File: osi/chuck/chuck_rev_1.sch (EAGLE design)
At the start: 3 parts

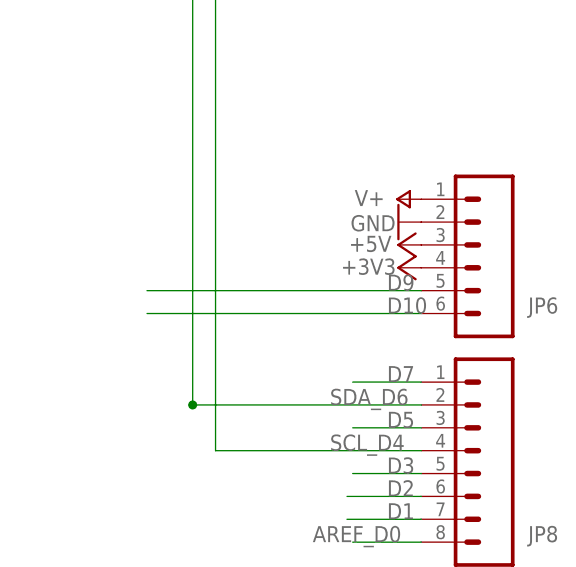
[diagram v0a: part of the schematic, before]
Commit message: D9 -> D8 for INT0
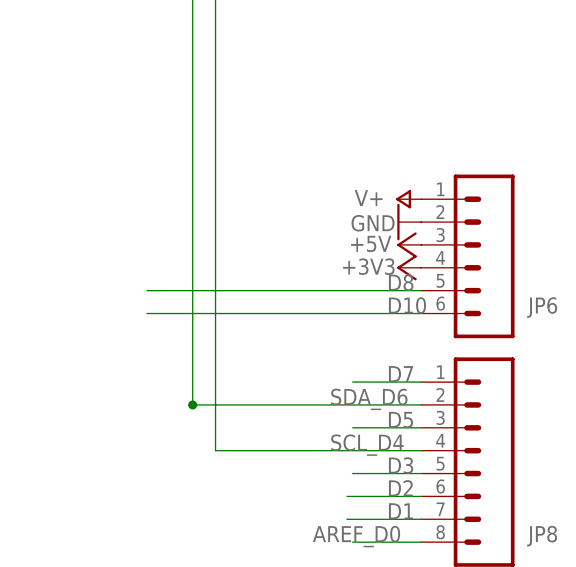
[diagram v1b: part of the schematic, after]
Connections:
- net D9 renamed D8
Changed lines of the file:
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@@
 </segment>
 </net>
-<net name="D9" class="0">
+<net name="D8" class="0">
 <segment>
 <wire x1="160.655" y1="86.36" x2="191.135" y2="86.36" width="0.1524" layer="91"/>

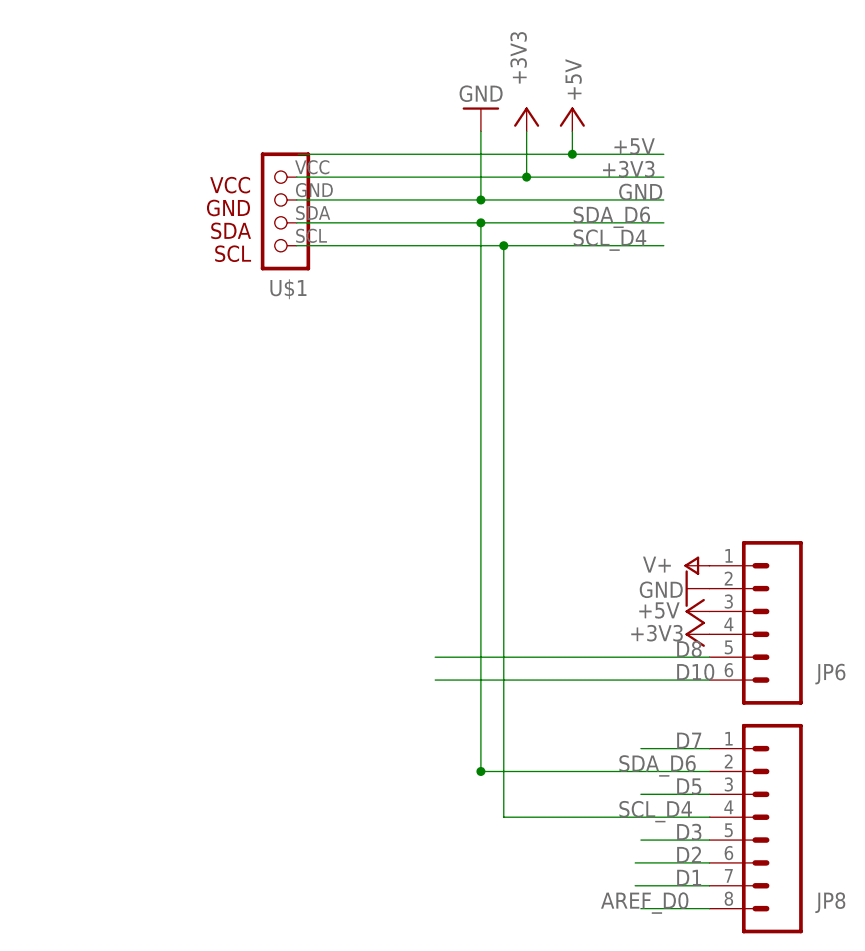
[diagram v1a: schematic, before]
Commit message: Moving RST line in brain
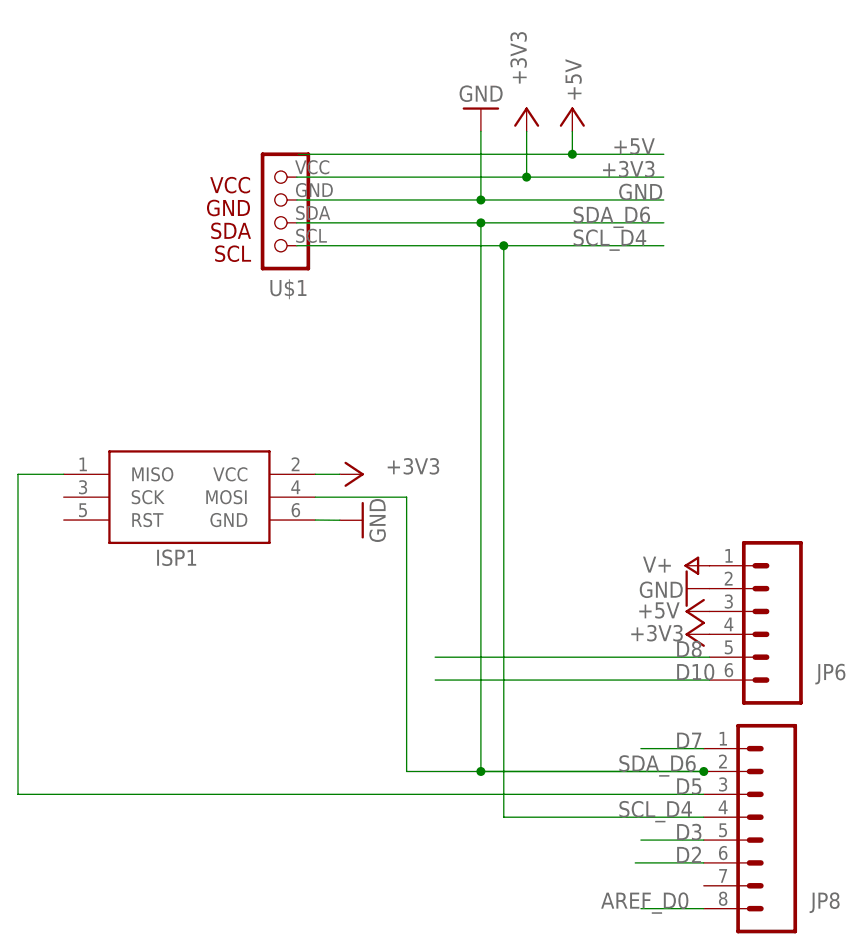
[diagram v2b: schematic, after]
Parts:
- added ISP1: AVRISP-6, adafruit_mod:AVRISP-6
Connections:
- removed net D1: JP8.7
- net +3V3: now also ISP1.VCC
- net D5: now also ISP1.MISO
- net GND: now also ISP1.GND
- net SDA_D6: now also ISP1.MOSI
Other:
- moved on the sheet: JP8
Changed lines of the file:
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@@
 <setting verticaltext="up"/>
 </settings>
-<grid distance="0.1" unitdist="inch" unit="inch" style="lines" multiple="1" display="no" altdistance="0.01" altunitdist="inch" altunit="inch"/>
+<grid distance="0.1" unitdist="inch" unit="inch" style="lines" multiple="1" display="no" altdistance="0.001" altunitdist="inch" altunit="inch"/>
 <layers>
 <layer number="1" name="Top" color="4" fill="1" visible="no" active="no"/>
@@
 <part name="FRAME1" library="SparkFun_mod" deviceset="FRAME-LETTER" device=""/>
 <part name="U$1" library="_my-parts" deviceset="NUNCHUCK" device="CHUCK"/>
+<part name="ISP1" library="adafruit_mod" deviceset="AVRISP" device="-6"/>
+<part name="+3V1" library="supply1" deviceset="+3V3" device=""/>
+<part name="GND1" library="SparkFun" deviceset="GND" device=""/>
 </parts>
 <sheets>
@@
 <attribute name="NAME" x="206.375" y="85.598" size="1.778" layer="95" rot="R180"/>
 </instance>
-<instance part="JP8" gate="G$1" x="196.215" y="68.58" smashed="yes" rot="R180">
-<attribute name="VALUE" x="201.295" y="81.28" size="1.778" layer="96" rot="R180"/>
-<attribute name="NAME" x="206.375" y="60.198" size="1.778" layer="95" rot="R180"/>
+<instance part="JP8" gate="G$1" x="195.58" y="68.58" smashed="yes" rot="R180">
+<attribute name="VALUE" x="200.66" y="81.28" size="1.778" layer="96" rot="R180"/>
+<attribute name="NAME" x="205.74" y="60.198" size="1.778" layer="95" rot="R180"/>
 </instance>
 <instance part="FRAME1" gate="G$1" x="0" y="0"/>
 <instance part="FRAME1" gate="G$2" x="147.32" y="0"/>
 <instance part="U$1" gate="G$1" x="147.828" y="142.24" rot="R180"/>
+<instance part="ISP1" gate="G$1" x="132.08" y="104.14"/>
+<instance part="+3V1" gate="G$1" x="152.6032" y="106.68" smashed="yes" rot="R270">
+<attribute name="VALUE" x="155.1432" y="106.68" size="1.778" layer="96"/>
+</instance>
+<instance part="GND1" gate="1" x="152.6032" y="101.5746" rot="R90"/>
 </instances>
 <busses>
@@
 <pinref part="JP6" gate="G$1" pin="2"/>
 </segment>
+<segment>
+<pinref part="ISP1" gate="G$1" pin="GND"/>
+<wire x1="147.32" y1="101.6" x2="150.0632" y2="101.5746" width="0.1524" layer="91"/>
+<pinref part="GND1" gate="1" pin="GND"/>
+</segment>
 </net>
 <net name="D3" class="0">
 <segment>
-<wire x1="191.135" y1="66.04" x2="183.515" y2="66.04" width="0.1524" layer="91"/>
+<wire x1="190.5" y1="66.04" x2="183.515" y2="66.04" width="0.1524" layer="91"/>
 <pinref part="JP8" gate="G$1" pin="5"/>
 <label x="187.325" y="66.04" size="1.778" layer="95"/>
@@
 <net name="D2" class="0">
 <segment>
-<wire x1="191.135" y1="63.5" x2="182.88" y2="63.5" width="0.1524" layer="91"/>
+<wire x1="190.5" y1="63.5" x2="182.88" y2="63.5" width="0.1524" layer="91"/>
 <pinref part="JP8" gate="G$1" pin="6"/>
 <label x="187.325" y="63.5" size="1.778" layer="95"/>
 </segment>
 </net>
-<net name="D1" class="0">
-<segment>
-<wire x1="191.135" y1="60.96" x2="182.88" y2="60.96" width="0.1524" layer="91"/>
-<pinref part="JP8" gate="G$1" pin="7"/>
-<label x="187.325" y="60.96" size="1.778" layer="95"/>
-</segment>
-</net>
 <net name="AREF_D0" class="0">
 <segment>
-<wire x1="191.135" y1="58.42" x2="183.515" y2="58.42" width="0.1524" layer="91"/>
+<wire x1="190.5" y1="58.42" x2="183.515" y2="58.42" width="0.1524" layer="91"/>
 <pinref part="JP8" gate="G$1" pin="8"/>
 <label x="179.07" y="58.42" size="1.778" layer="95"/>
@@
 <segment>
 <wire x1="186.055" y1="134.62" x2="165.735" y2="134.62" width="0.1524" layer="91"/>
-<wire x1="165.735" y1="73.66" x2="191.135" y2="73.66" width="0.1524" layer="91"/>
+<wire x1="165.735" y1="73.66" x2="190.5" y2="73.66" width="0.1524" layer="91"/>
 <wire x1="165.735" y1="134.62" x2="165.735" y2="73.66" width="0.1524" layer="91"/>
 <junction x="165.735" y="73.66"/>
@@
 <pinref part="U$1" gate="G$1" pin="SDA"/>
 <wire x1="145.288" y1="134.62" x2="165.735" y2="134.62" width="0.1524" layer="91"/>
+<wire x1="190.5" y1="73.66" x2="157.48" y2="73.66" width="0.1524" layer="91"/>
+<wire x1="157.48" y1="73.66" x2="157.48" y2="104.14" width="0.1524" layer="91"/>
+<junction x="190.5" y="73.66"/>
+<pinref part="ISP1" gate="G$1" pin="MOSI"/>
+<wire x1="157.48" y1="104.14" x2="147.32" y2="104.14" width="0.1524" layer="91"/>
 </segment>
 </net>
 <net name="D5" class="0">
 <segment>
-<wire x1="183.515" y1="71.12" x2="191.135" y2="71.12" width="0.1524" layer="91"/>
 <pinref part="JP8" gate="G$1" pin="3"/>
 <label x="187.325" y="71.12" size="1.778" layer="95"/>
+<wire x1="190.5" y1="71.12" x2="114.3" y2="71.12" width="0.1524" layer="91"/>
+<wire x1="114.3" y1="71.12" x2="114.3" y2="106.68" width="0.1524" layer="91"/>
+<pinref part="ISP1" gate="G$1" pin="MISO"/>
+<wire x1="114.3" y1="106.68" x2="119.38" y2="106.68" width="0.1524" layer="91"/>
 </segment>
 </net>
@@
 <segment>
 <wire x1="186.055" y1="132.08" x2="168.275" y2="132.08" width="0.1524" layer="91"/>
-<wire x1="168.275" y1="68.58" x2="191.135" y2="68.58" width="0.1524" layer="91"/>
+<wire x1="168.275" y1="68.58" x2="190.5" y2="68.58" width="0.1524" layer="91"/>
 <wire x1="168.275" y1="132.08" x2="168.275" y2="68.58" width="0.1524" layer="91"/>
 <junction x="168.275" y="132.08"/>
@@
 <net name="D7" class="0">
 <segment>
-<wire x1="183.515" y1="76.2" x2="191.135" y2="76.2" width="0.1524" layer="91"/>
+<wire x1="183.515" y1="76.2" x2="190.5" y2="76.2" width="0.1524" layer="91"/>
 <pinref part="JP8" gate="G$1" pin="1"/>
 <label x="187.325" y="76.2" size="1.778" layer="95"/>
@@
 <pinref part="JP6" gate="G$1" pin="4"/>
 </segment>
-</net>
+<segment>
+<pinref part="ISP1" gate="G$1" pin="VCC"/>
+<wire x1="147.32" y1="106.68" x2="150.0632" y2="106.68" width="0.1524" layer="91"/>
+<pinref part="+3V1" gate="G$1" pin="+3V3"/>
+</segment>
+</net>
